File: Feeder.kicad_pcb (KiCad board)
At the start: 4 copper layers, 91 x 85 mm, 107 parts, among them J101 Conn_02x03_Odd_Even, J102 Conn_01x03_Pin, J103 Conn_01x02_Pin, U101 XBLW 24C02S(XBLW), U201 CMP6793RE, U301 CMP6793RE, U601 TPS562202, U701 TPS562202

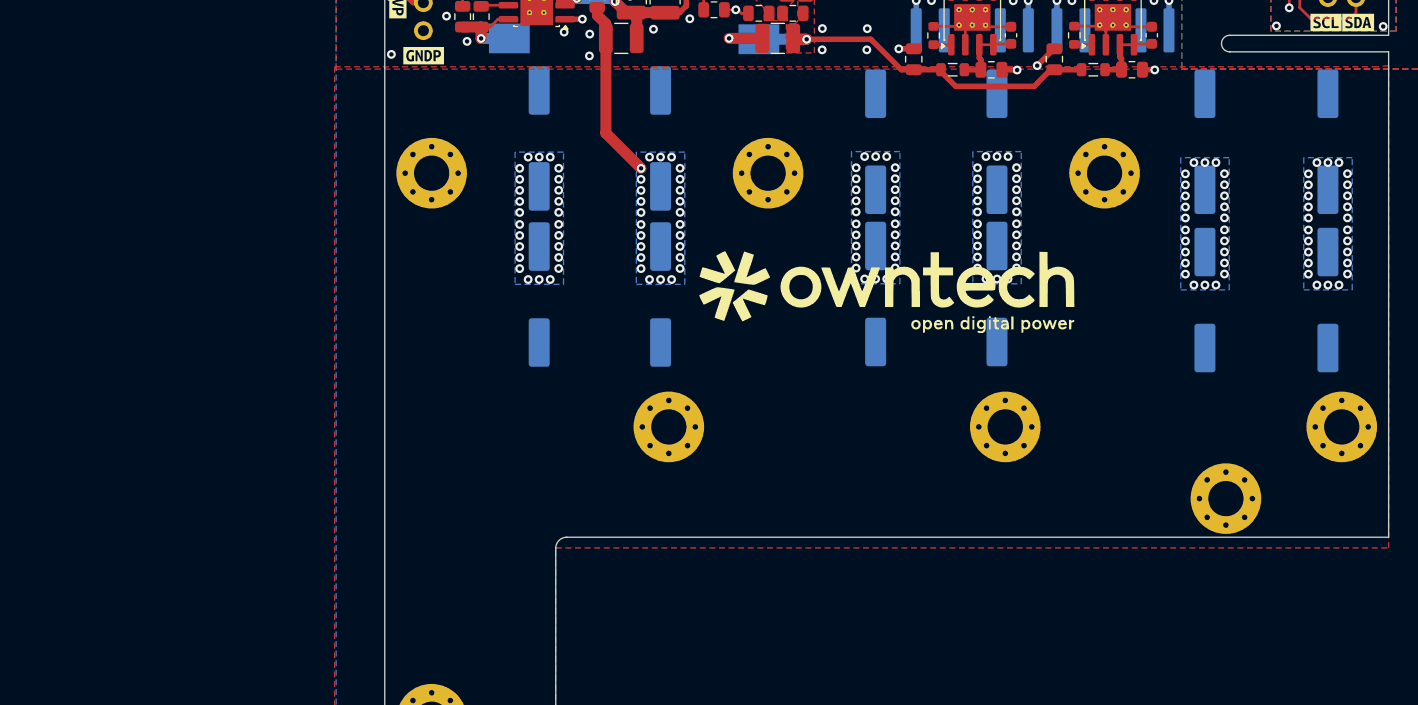
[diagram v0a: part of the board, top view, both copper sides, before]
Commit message: moved capacitors
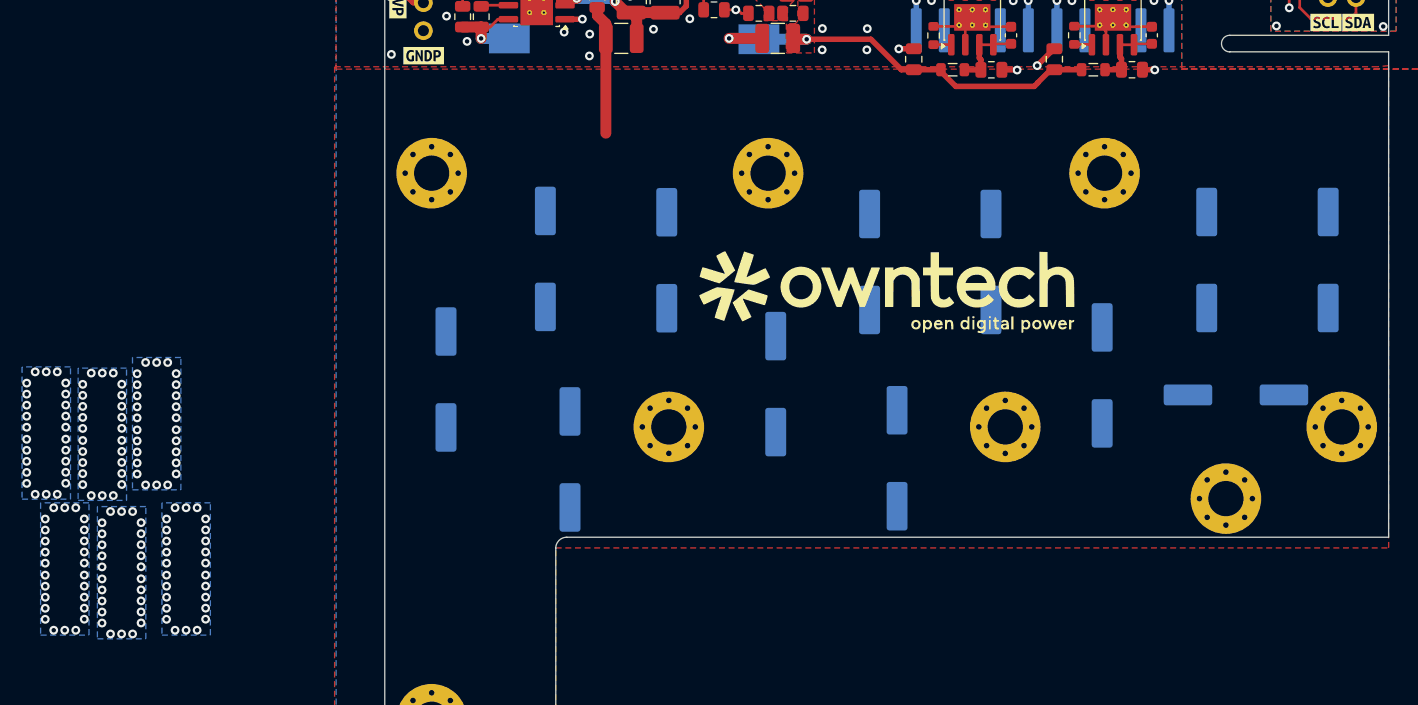
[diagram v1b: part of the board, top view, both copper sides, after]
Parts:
- moved C110 23.4 mm to (10.1, -44.3), turned to -90 degrees
- moved C113 17.4 mm to (50.9, -37.2)
- moved C109 15.2 mm to (21.3, -37.0)
- moved C108 15.1 mm to (19.1, -55.2)
- moved C111 12.2 mm to (39.9, -43.9)
- moved C115 12.0 mm to (81.7, -42.9), turned to 180 degrees
- moved C117 11.6 mm to (69.5, -44.7)
- moved C112 10.9 mm to (48.5, -55.0)
- moved C114 10.9 mm to (59.5, -55.0)
- moved C118 10.7 mm to (79.0, -55.1)
- moved C116 10.7 mm to (90.0, -55.1)
- moved C107 3.16 mm to (30.1, -55.1), turned to 90 degrees
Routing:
- net /VHigh: track 16.2 -> 11.7 mm
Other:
- board text added: "tall zone"

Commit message: v2 wip
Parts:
- removed J103: Conn_01x02_Pin, Connector_PinHeader_2.54mm:PinHeader_1x02_P2.54mm_Vertical
- removed R201, R301: R_Small, Resistor_SMD:R_0603_1608Metric
- added C801: 10uF, Capacitor_SMD:C_0805_2012Metric, B.Cu at (52.8, -93.2)
- added C802: 10uF, Capacitor_SMD:C_0805_2012Metric, F.Cu at (50.0, -95.7)
- added C803: 100nF, Capacitor_SMD:C_0603_1608Metric, F.Cu at (50.0, -93.9)
- added C804: 10uF, Capacitor_SMD:C_0805_2012Metric, F.Cu at (50.8, -70.3)
- added D101: LED, LED_SMD:LED_0402_1005Metric, F.Cu at (25.8, -93.6)
- added D102: LED, LED_SMD:LED_0402_1005Metric, F.Cu at (28.3, -93.6)
- added D103: LED, LED_SMD:LED_0402_1005Metric, F.Cu at (30.8, -93.6)
- added D801: PMEG4010, Diode_SMD:D_SOD-882, B.Cu at (44.9, -69.7)
- added D802: PMEG4010, Diode_SMD:D_SOD-882, B.Cu at (55.1, -69.9)
- added JP101: Jumper_3_Open, Connector_PinHeader_2.54mm:PinHeader_1x03_P2.54mm_Vertical, F.Cu at (85.7, -93.2)
- added JP102: Jumper_2_Bridged, Footprints:SolderJumper-2_P1.3mm_Bridged_RoundedPad1.0x1.5mm, B.Cu at (25.8, -91.0)
- added JP103: Jumper_2_Bridged, Footprints:SolderJumper-2_P1.3mm_Bridged_RoundedPad1.0x1.5mm, B.Cu at (28.3, -91.0)
- added JP104: Jumper_2_Bridged, Footprints:SolderJumper-2_P1.3mm_Bridged_RoundedPad1.0x1.5mm, B.Cu at (30.8, -91.0)
- added JP105: Jumper_3_Open, Connector_PinHeader_2.54mm:PinHeader_1x03_P2.54mm_Vertical, F.Cu at (9.02, -131.0)
- added L801: 10uH, Inductor_SMD:L_0805_2012Metric, B.Cu at (50.0, -94.2)
- added Q201: 2N7002, Package_TO_SOT_SMD:SOT-23, F.Cu at (79.9, -69.0)
- added Q301: 2N7002, Package_TO_SOT_SMD:SOT-23, F.Cu at (67.2, -69.0)
- added Q401: 2N7002, Package_TO_SOT_SMD:SOT-23, F.Cu at (-14.0, -88.4)
- added Q501: 2N7002, Package_TO_SOT_SMD:SOT-23, F.Cu at (-14.0, -75.1)
- added Q901: BC857BS, Package_TO_SOT_SMD:SOT-363_SC-70-6, F.Cu at (2.31, -122.6)
- added Q902: AO3401A, Package_TO_SOT_SMD:SOT-23, F.Cu at (2.80, -126.1)
- added Q903: BC857BS, Package_TO_SOT_SMD:SOT-363_SC-70-6, F.Cu at (7.05, -122.7)
- added Q904: AO3401A, Package_TO_SOT_SMD:SOT-23, F.Cu at (7.48, -126.1)
- added R107: 2k2, Resistor_SMD:R_0402_1005Metric, B.Cu at (25.8, -93.6)
- added R110: 1k, Resistor_SMD:R_0402_1005Metric, B.Cu at (28.3, -93.6)
- added R111: 1k, Resistor_SMD:R_0402_1005Metric, B.Cu at (30.8, -93.6)
- added R203: R_Small, Resistor_SMD:R_0603_1608Metric, F.Cu at (72.0, -69.8)
- added R204: 4.7k, Resistor_SMD:R_0603_1608Metric, F.Cu at (76.5, -90.3)
- added R303: R_Small, Resistor_SMD:R_0603_1608Metric, F.Cu at (59.2, -69.8)
- added R304: 4.7k, Resistor_SMD:R_0603_1608Metric, F.Cu at (63.8, -90.3)
- added R405: 499k, Footprints:R_0805_2012Metric, B.Cu at (-17.0, -86.7)
- added R406: 499k, Footprints:R_0805_2012Metric, B.Cu at (-17.0, -83.6)
- added R407: 143k, Footprints:R_0805_2012Metric, B.Cu at (-18.0, -89.2)
- added R505: 499k, Footprints:R_0805_2012Metric, B.Cu at (-17.0, -73.3)
- added R506: 499k, Footprints:R_0805_2012Metric, B.Cu at (-17.0, -70.2)
- added R507: 143k, Footprints:R_0805_2012Metric, B.Cu at (-18.0, -75.8)
- added R801: R_Small, Resistor_SMD:R_0603_1608Metric, F.Cu at (53.5, -90.8)
- added R802: 4.7k, Resistor_SMD:R_0603_1608Metric, F.Cu at (49.0, -70.3)
- added R901: 10k, Resistor_SMD:R_0603_1608Metric, F.Cu at (1.76, -120.4)
- added R902: 10k, Resistor_SMD:R_0603_1608Metric, F.Cu at (0.38, -122.7)
- added R903: 10k, Resistor_SMD:R_0603_1608Metric, F.Cu at (6.51, -120.4)
- added R904: 10k, Resistor_SMD:R_0603_1608Metric, F.Cu at (5.16, -122.7)
- added TR801: CMT88F0U, feeder:CMT88F0U, B.Cu at (50.0, -80.3)
- added U801: CMP6793RE, Package_SO:SOIC-8-1EP_3.9x4.9mm_P1.27mm_EP2.41x3.3mm_ThermalVias, F.Cu at (50.0, -89.4)
- C103, C104, C105, C106, C201, C301, C702, L101, L201, L301: moved to B.Cu
- C204, C304: moved to F.Cu
- R101: value 10k -> 22k; footprint Capacitor_SMD:C_0603_1608Metric -> Footprints:R_0805_2012Metric
- R202, R302: value 4.7k -> 100k; moved to F.Cu
- moved C601 119.6 mm to (-26.8, -115.3)
- moved C603 119.6 mm to (-26.1, -108.9)
- moved R601 119.6 mm to (-27.4, -110.8)
- moved U601 119.6 mm to (-26.9, -113.3)
- moved C602 119.6 mm to (-26.7, -111.1)
- moved L601 119.6 mm to (-30.7, -110.8)
- moved R602 119.6 mm to (-27.3, -109.1)
- moved C104 88.3 mm to (-56.1, -52.9), turned to 180 degrees
- moved C106 86.6 mm to (-51.1, -53.0), turned to 0 degrees
- moved C103 84.9 mm to (-55.0, -56.5), turned to -90 degrees
- moved C105 84.6 mm to (-51.7, -56.5), turned to -90 degrees
- moved L101 80.4 mm to (-53.3, -61.6), turned to -90 degrees
- moved C102 80.1 mm to (-53.3, -61.4), turned to -90 degrees
- moved C101 78.4 mm to (-53.3, -64.5), turned to -90 degrees
- moved R101 71.1 mm to (19.6, -109.4), turned to 0 degrees
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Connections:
- C202 pad 1: Net-(U201-EN) -> Net-(U201-VCC)
- C203 pad 1: Net-(U201-EN) -> Net-(U201-VCC)
- C204 pad 1: +12V_DGND -> /dc-dc_isolated_disabling/VOUT
- C302 pad 1: Net-(U301-EN) -> Net-(U301-VCC)
- C303 pad 1: Net-(U301-EN) -> Net-(U301-VCC)
- C304 pad 1: +12V_DGND -> /dc-dc_isolated_disabling/VOUT
- C503 pad 2: +12V_PGND -> /12V_PWR_BUS
- C504 pad 1: +12V_PGND -> /12V_PWR_BUS
- D201 pad 1: +12V_DGND -> /dc-dc_isolated_disabling/VOUT
- D202 pad 1: +12V_DGND -> /dc-dc_isolated_disabling/VOUT
- D301 pad 1: +12V_DGND -> /dc-dc_isolated_disabling/VOUT
- D302 pad 1: +12V_DGND -> /dc-dc_isolated_disabling/VOUT
- L201 pad 2: Net-(U201-EN) -> Net-(U201-VCC)
- L301 pad 2: Net-(U301-EN) -> Net-(U301-VCC)
- L501 pad 2: +12V_PGND -> /12V_PWR_BUS
- R101 pad 1: +5V_DGND -> +12V_PGND
- R101 pad 2: /WP -> /buck/~{EN}
- R202 pad 1: +12V_DGND -> Net-(U201-VCC)
- R202 pad 2: DGND -> Net-(Q201-D)
- R302 pad 1: +12V_DGND -> Net-(U301-VCC)
- R302 pad 2: DGND -> Net-(Q301-D)
- R503 pad 1: +12V_PGND -> /12V_PWR_BUS
- U101 pad 5: /WP -> DGND
- U201 pad 3: Net-(U201-EN) -> Net-(U201-VCC)
- U201 pad 4: Net-(U201-EN) -> Net-(Q201-D)
- U301 pad 3: Net-(U301-EN) -> Net-(U301-VCC)
- U301 pad 4: Net-(U301-EN) -> Net-(Q301-D)
- U401 pad 3: /VIN_{FILT} -> Net-(Q401-D)
- U501 pad 3: /VIN_{FILT} -> Net-(Q501-D)
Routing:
- net +12V_DGND: track 62.0 -> 0.00 mm, vias 1 -> 0
- net /12V_P_0: track 33.1 -> 0.00 mm, vias 1 -> 0
- net /VIN_{FILT}: track 26.4 -> 6.79 mm
- net DGND: track 9.39 -> 24.2 mm, vias 22 -> 10
- net /WP: track 11.9 -> 0.00 mm
- net /VHigh: track 11.7 -> 0.00 mm
- net +5V_DGND: track 16.5 -> 4.95 mm, vias 1 -> 0
- net +5V_PGND: track 20.4 -> 10.3 mm
- net /dc-dc_isolated_disabling/VOUT: track 0.00 -> 9.48 mm, vias 0 -> 4
- net Net-(U601-VFB): track 8.42 -> 0.00 mm, vias 1 -> 0
- net Net-(U601-SW): track 6.90 -> 0.00 mm
- net Net-(U201-EN): track 6.74 -> 0.00 mm
- net Net-(U301-EN): track 6.74 -> 0.00 mm
- net Net-(U301-VCC): track 0.00 -> 5.71 mm
- net Net-(U201-VCC): track 0.00 -> 5.71 mm
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- added copper zone on B.Cu, net /dc-dc_isolated_disabling/VOUT
- removed copper zone on F.Cu, net +12V_PGND
- removed copper zone on F.Cu, net /12V_P_0
- removed copper zone on F.Cu, net Net-(C103-Pad2)
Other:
- outline, holes or cut-outs redrawn

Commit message: First layout complete - DRC not clear yet.
Signed-off-by: Jean Alinei <jean.alinei@owntech.org>
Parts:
- removed the kibuzzard-6A7463BC at (87.7, -81.3)
- C101, C102, C119, C602, R901, R902, U101: moved to B.Cu
- U401, U501: footprint Package_SO:Texas_R-PDSO-G8_EP2.95x4.9mm_Mask2.4x3.1mm_ThermalVias -> Footprints:Texas_R-PDSO-G8_EP2.95x4.9mm_Mask2.4x3.1mm_ThermalVias
- moved L601 128.2 mm to (92.3, -74.7), turned to 90 degrees
- moved C601 124.5 mm to (89.6, -71.3), turned to 180 degrees
- moved U601 122.3 mm to (88.7, -73.2), turned to 180 degrees
- moved C602 122.1 mm to (89.7, -74.2), turned to -90 degrees
- moved R602 120.5 mm to (87.0, -71.2)
- moved C603 119.5 mm to (88.9, -76.4), turned to -90 degrees
- moved R601 119.2 mm to (85.9, -73.6), turned to -90 degrees
- moved C102 94.5 mm to (40.6, -71.8), turned to 0 degrees
- moved C101 91.1 mm to (37.5, -71.8), turned to 0 degrees
- moved C103 89.1 mm to (30.7, -80.9), turned to 180 degrees
- moved L101 87.6 mm to (33.6, -71.9), turned to 180 degrees
- moved C104 86.9 mm to (26.2, -80.8)
- moved C105 83.2 mm to (30.8, -67.4), turned to 180 degrees
- moved C106 78.8 mm to (26.3, -67.3), turned to 180 degrees
- moved L701 69.8 mm to (14.3, -72.0), turned to 90 degrees
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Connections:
- J101 pad 1: +12V_DGND -> /SDA
- J101 pad 2: +5V_DGND -> /SCL
- J101 pad 5: /SDA -> +12V_DGND
- J101 pad 6: /SCL -> +5V_DGND
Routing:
- net /buck/~{EN}: track 0.00 -> 107.9 mm, vias 0 -> 4
- net /12V_P_0: track 0.00 -> 97.8 mm, vias 0 -> 8
- net /12V_DIGI_TO_POWER: track 3.62 -> 73.9 mm, vias 0 -> 8
- net +12V_PGND: track 19.6 -> 55.4 mm, vias 2 -> 8
- net /VHigh: track 0.00 -> 26.5 mm, vias 156 -> 0
- net /VIN_{FILT}: track 6.79 -> 25.0 mm
- net +5V_DGND: track 4.95 -> 22.9 mm, vias 0 -> 1
- net PGND: track 53.4 -> 36.2 mm, vias 19 -> 17
- net /12V_PWR_BUS: track 3.65 -> 14.6 mm, vias 0 -> 7
- net /SDA: track 8.59 -> 18.1 mm, vias 0 -> 1
- net +12V_DGND: track 0.00 -> 9.40 mm, vias 0 -> 4
- net Net-(Q501-D): track 1.77 -> 10.4 mm, vias 0 -> 1
- net Net-(Q401-D): track 1.77 -> 8.99 mm, vias 0 -> 1
- net Net-(Q901B-C2): track 3.05 -> 8.22 mm, vias 0 -> 2
- net Net-(U601-VBST): track 0.00 -> 5.11 mm, vias 0 -> 1
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- added copper zone on B.Cu, net +12V_DGND
- added copper zone on F.Cu, net +12V_DGND
- added copper zone on F.Cu, net +12V_PGND
- added copper zone on F.Cu, net +5V_DGND
- added copper zone on F.Cu, net +5V_PGND
- added copper zone on B.Cu, net /12V_DIGI_TO_POWER
- added copper zone on F.Cu, net /12V_DIGI_TO_POWER
- added copper zone on F.Cu, net /12V_PWR_BUS
- added copper zone on F.Cu, net /12V_P_0
- added copper zone on In1.Cu, net /VHigh
- added copper zone on In2.Cu, net /VHigh
- added copper zone on F.Cu, net /VIN_{FILT}
- added copper zone on B.Cu, net /dc-dc_isolated/VIN
- added copper zone on F.Cu, net /dc-dc_isolated/VIN
- added copper zone on In1.Cu, net DGND
- added copper zone on In2.Cu, net DGND
- added copper zone on F.Cu, net Net-(U201-VD1)
- added copper zone on F.Cu, net Net-(U201-VD2)
- added copper zone on F.Cu, net Net-(U301-VD1)
- added copper zone on F.Cu, net Net-(U301-VD2)
- added copper zone on F.Cu, net Net-(U601-SW)
- added copper zone on F.Cu, net Net-(U701-SW)
- added copper zone on F.Cu, net Net-(U801-EN)
- added copper zone on F.Cu, net Net-(U801-VD1)
- added copper zone on F.Cu, net Net-(U801-VD2)
- added copper zone on In1.Cu, net PGND
- added copper zone on In2.Cu, net PGND
- removed copper zone on F.Cu, net /VHigh
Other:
- outline, holes or cut-outs redrawn

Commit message: Slowly updating the feeder board
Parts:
- added ?: , , F.Cu at (22.2, -59.0)
- added ?: , , F.Cu at (59.8, -59.0)
- added ?: , , F.Cu at (83.2, -59.0)
- added ?: , , F.Cu at (90.2, -59.0)
- added ?: , , F.Cu at (29.2, -59.0)
- added ?: , , F.Cu at (52.8, -59.0)
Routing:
- net /VHigh: track 26.5 -> 34.5 mm
- net /12V_DIGI_TO_POWER: track 73.9 -> 76.2 mm

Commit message: updated gitignore and wip on the pcb. modified the functionnal diagram on the schematic
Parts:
- removed the ? at (22.2, -59.0)
- removed the ? at (59.8, -59.0)
- removed the ? at (83.2, -59.0)
- removed the ? at (90.2, -59.0)
- removed the ? at (29.2, -59.0)
- removed the ? at (52.8, -59.0)
- added ?: , , F.Cu at (90.2, -63.0)
- added ?: , , F.Cu at (22.2, -63.0)
- added ?: , , F.Cu at (83.2, -63.0)
- added ?: , , F.Cu at (29.2, -63.0)
- added ?: , , F.Cu at (52.8, -63.0)
- added ?: , , F.Cu at (59.8, -63.0)
- U401, U501: value ~ -> LM5169PDDAR
- moved C116 1.38 mm to (90.0, -53.8)
- moved C107 1.36 mm to (30.1, -53.8)
- moved C114 1.20 mm to (59.5, -53.8)
- moved R101 1.09 mm to (28.2, -90.9)
- moved C117 0.67 mm to (69.5, -44.0)
- moved C302 0.53 mm to (63.2, -65.0)
- moved Q301 0.48 mm to (67.2, -69.5)
- moved R302 0.48 mm to (65.9, -66.8)
- moved C110 0.30 mm to (10.1, -44.0)
- moved C115 0.16 mm to (81.5, -42.9)
- moved C111 0.12 mm to (39.9, -44.0)
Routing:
- net /VHigh: track 34.5 -> 9.83 mm
- net /12V_P_0: track 97.8 -> 79.2 mm
- net PGND: track 36.2 -> 42.5 mm
- net /12V_DIGI_TO_POWER: track 76.2 -> 79.1 mm
- net /buck/~{EN}: track 107.9 -> 109.2 mm
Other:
- outline, holes or cut-outs redrawn

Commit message: small tweaks, silkscreen, component placements
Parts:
- added kibuzzard-6A957D2D: G***, kibuzzard-6A957D2D, F.Cu at (30.8, -89.4)
- added kibuzzard-6A957D2D: G***, kibuzzard-6A957D2D, F.Cu at (83.6, -89.4)
- added kibuzzard-6A957D3B: G***, kibuzzard-6A957D3B, F.Cu at (28.3, -91.0)
- added kibuzzard-6A957D3B: G***, kibuzzard-6A957D3B, F.Cu at (81.2, -91.1)
- added kibuzzard-6A957F06: G***, kibuzzard-6A957F06, F.Cu at (12.5, -90.7)
- added kibuzzard-6A957F58: G***, kibuzzard-6A957F58, F.Cu at (16.3, -90.9)
- added kibuzzard-6A957FC9: G***, kibuzzard-6A957FC9, F.Cu at (24.1, -90.9)
- R101: moved to B.Cu
- R107: moved to F.Cu
- R110, R111: value 1k -> 2k2; moved to F.Cu
- moved R111 8.74 mm to (15.5, -93.1), turned to 0 degrees
- moved D103 8.72 mm to (15.5, -94.1), turned to 180 degrees
- moved JP102 8.19 mm to (22.5, -93.6)
- moved R107 7.70 mm to (22.5, -93.1), turned to 0 degrees
- moved JP104 6.76 mm to (15.5, -93.6)
- moved D101 6.35 mm to (22.5, -94.1), turned to 180 degrees
- moved R101 3.18 mm to (31.4, -90.9)
- moved R110 1.27 mm to (19.0, -93.1), turned to 0 degrees
- moved D102 1.18 mm to (19.0, -94.1), turned to 180 degrees
- moved JP103 0.85 mm to (19.0, -93.6)
- moved R401 0.29 mm to (26.9, -88.0)
- moved R901 0.06 mm to (7.52, -86.3)
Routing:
- net /buck/~{EN}: track 109.2 -> 101.3 mm
- net /12V_DIGI_TO_POWER: track 79.1 -> 72.3 mm, vias 8 -> 6
- net PGND: track 42.5 -> 47.4 mm, vias 17 -> 31
- net Net-(D101-A): track 4.05 -> 0.98 mm, vias 1 -> 0
- net +12V_PGND: track 55.0 -> 57.5 mm, vias 8 -> 6
- net Net-(D102-A): track 3.35 -> 1.02 mm, vias 1 -> 0
- net Net-(D103-A): track 1.95 -> 1.02 mm, vias 1 -> 0
- net Net-(JP103-B): track 1.51 -> 2.27 mm, vias 0 -> 1
- net /12V_PWR_BUS: track 14.6 -> 15.4 mm
- net Net-(JP102-B): track 1.41 -> 2.09 mm, vias 0 -> 1
- net Net-(JP104-B): track 1.55 -> 1.51 mm, vias 0 -> 1
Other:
- board text added: "12V D->P"
- board text added: "12V High->P"
- board text added: "BUCK EN"
